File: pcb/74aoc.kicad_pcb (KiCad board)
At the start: 2 copper layers, 72 parts, among them J1 Conn_01x02_Pin, J2 Conn_01x06_Pin, U1 MC74HC151ADTR2G, U2 SN74LVC1G74, U3 AMS1117-3.3, U5 SN74HC595PWR, U6 SN74HC595PWR

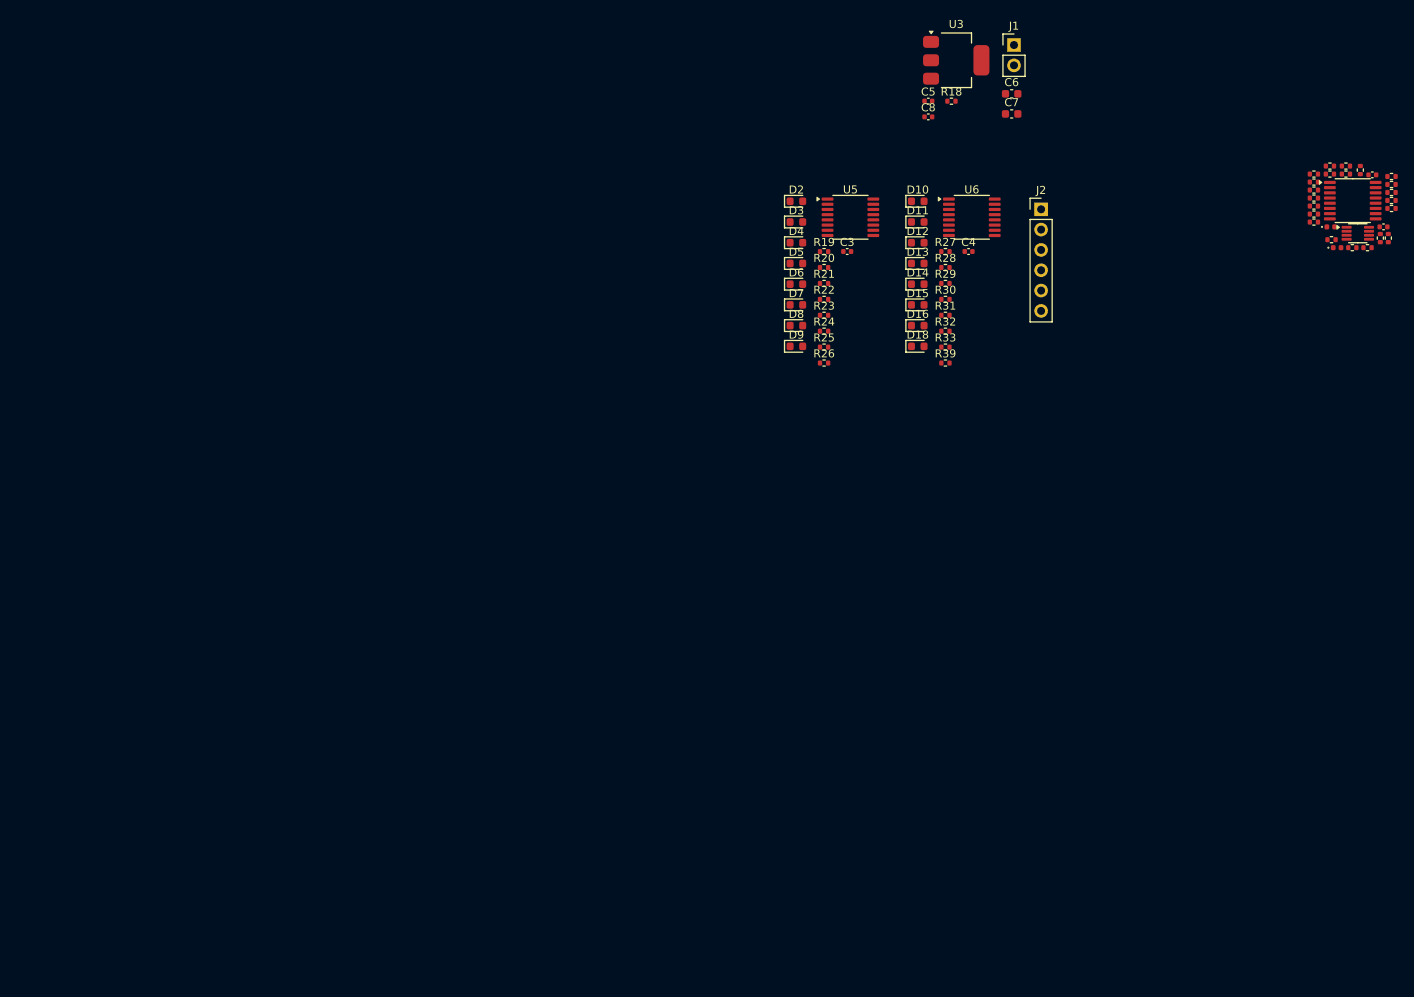
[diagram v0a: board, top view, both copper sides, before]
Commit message: Remove IO shift registers
Too complex
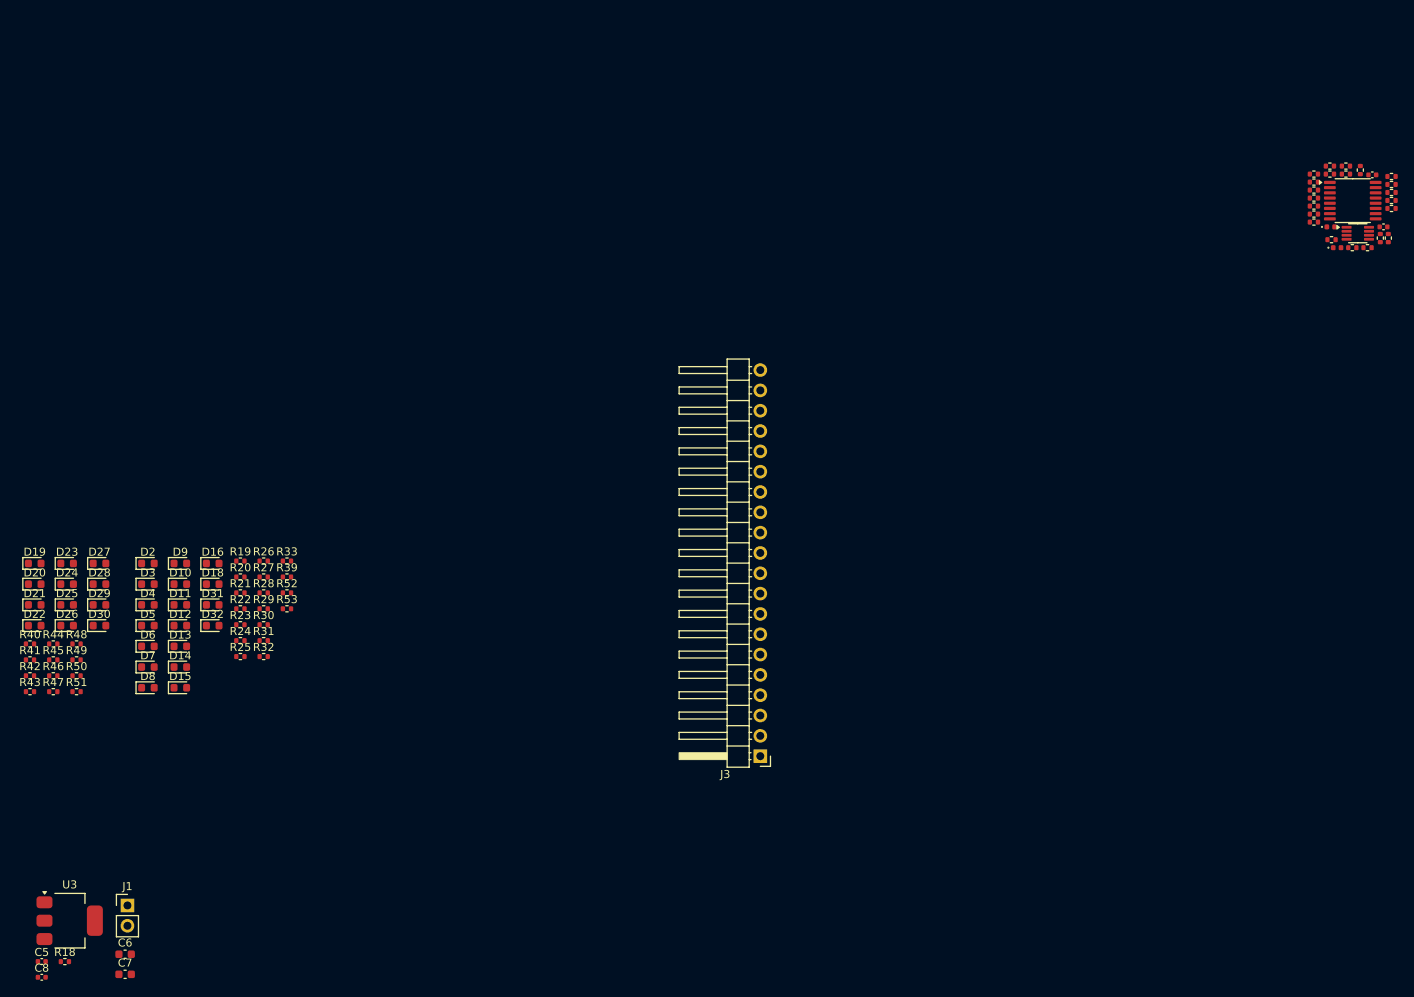
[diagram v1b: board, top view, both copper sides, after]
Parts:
- removed C3, C4: 100n, Capacitor_SMD:C_0402_1005Metric
- removed J2: Conn_01x06_Pin, Connector_PinHeader_2.54mm:PinHeader_1x06_P2.54mm_Vertical
- removed U5, U6: SN74HC595PWR, Package_SO:TSSOP-16_4.4x5mm_P0.65mm
- added D19: LED, LED_SMD:LED_0603_1608Metric, F.Cu at (-59.0, 143.4)
- added D20: LED, LED_SMD:LED_0603_1608Metric, F.Cu at (-59.0, 146.0)
- added D21: LED, LED_SMD:LED_0603_1608Metric, F.Cu at (-59.0, 148.6)
- added D22: LED, LED_SMD:LED_0603_1608Metric, F.Cu at (-59.0, 151.1)
- added D23: LED, LED_SMD:LED_0603_1608Metric, F.Cu at (-55.0, 143.4)
- added D24: LED, LED_SMD:LED_0603_1608Metric, F.Cu at (-55.0, 146.0)
- added D25: LED, LED_SMD:LED_0603_1608Metric, F.Cu at (-55.0, 148.6)
- added D26: LED, LED_SMD:LED_0603_1608Metric, F.Cu at (-55.0, 151.1)
- added D27: LED, LED_SMD:LED_0603_1608Metric, F.Cu at (-50.9, 143.4)
- added D28: LED, LED_SMD:LED_0603_1608Metric, F.Cu at (-50.9, 146.0)
- added D29: LED, LED_SMD:LED_0603_1608Metric, F.Cu at (-50.9, 148.6)
- added D30: LED, LED_SMD:LED_0603_1608Metric, F.Cu at (-50.9, 151.1)
- added D31: LED, LED_SMD:LED_0603_1608Metric, F.Cu at (-36.8, 148.6)
- added D32: LED, LED_SMD:LED_0603_1608Metric, F.Cu at (-36.8, 151.1)
- added J3: Conn_01x20_Pin, Connector_PinHeader_2.54mm:PinHeader_1x20_P2.54mm_Horizontal, F.Cu at (31.7, 167.5)
- added R40: 10k, Resistor_SMD:R_0402_1005Metric, F.Cu at (-59.6, 153.4)
- added R41: 10k, Resistor_SMD:R_0402_1005Metric, F.Cu at (-59.6, 155.4)
- added R42: 10k, Resistor_SMD:R_0402_1005Metric, F.Cu at (-59.6, 157.4)
- added R43: 10k, Resistor_SMD:R_0402_1005Metric, F.Cu at (-59.6, 159.4)
- added R44: 10k, Resistor_SMD:R_0402_1005Metric, F.Cu at (-56.7, 153.4)
- added R45: 10k, Resistor_SMD:R_0402_1005Metric, F.Cu at (-56.7, 155.4)
- added R46: 10k, Resistor_SMD:R_0402_1005Metric, F.Cu at (-56.7, 157.4)
- added R47: 10k, Resistor_SMD:R_0402_1005Metric, F.Cu at (-56.7, 159.4)
- added R48: 10k, Resistor_SMD:R_0402_1005Metric, F.Cu at (-53.8, 153.4)
- added R49: 10k, Resistor_SMD:R_0402_1005Metric, F.Cu at (-53.8, 155.4)
- added R50: 10k, Resistor_SMD:R_0402_1005Metric, F.Cu at (-53.8, 157.4)
- added R51: 10k, Resistor_SMD:R_0402_1005Metric, F.Cu at (-53.8, 159.4)
- added R52: 10k, Resistor_SMD:R_0402_1005Metric, F.Cu at (-27.5, 147.1)
- added R53: 10k, Resistor_SMD:R_0402_1005Metric, F.Cu at (-27.5, 149.0)
- moved C5 154.4 mm to (-58.1, 193.1)
- moved C6 154.4 mm to (-47.7, 192.2)
- moved C7 154.4 mm to (-47.7, 194.7)
- moved C8 154.4 mm to (-58.1, 195.1)
- moved J1 154.4 mm to (-47.4, 186.1)
- moved R18 154.4 mm to (-55.2, 193.1)
- moved U3 154.4 mm to (-54.6, 188.0)
- moved D10 103.9 mm to (-40.8, 146.0)
- moved D11 103.9 mm to (-40.8, 148.6)
- moved D14 103.9 mm to (-40.8, 156.3)
- moved D15 103.9 mm to (-40.8, 158.9)
- moved D12 103.9 mm to (-40.8, 151.1)
- moved D13 103.9 mm to (-40.8, 153.7)
- moved R28 94.4 mm to (-30.4, 147.1)
- moved R31 94.4 mm to (-30.4, 153.0)
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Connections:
- R19 pad 1: W_IO_O1 -> W_IO_I0
- R20 pad 1: W_IO_O2 -> W_IO_I1
- R21 pad 1: W_IO_O3 -> W_IO_I2
- R22 pad 1: W_IO_O4 -> W_IO_I3
- R23 pad 1: W_IO_O5 -> W_IO_I4
- R24 pad 1: W_IO_O6 -> W_IO_I5
- R25 pad 1: W_IO_O7 -> W_IO_I6
- R26 pad 1: W_IO_O0 -> W_IO_I7
- R27 pad 1: W_IO_O9 -> W_IO_I8
- R28 pad 1: W_IO_O10 -> W_IO_I9
- R29 pad 1: W_IO_O11 -> W_IO_I10
- R30 pad 1: W_IO_O12 -> W_IO_I11
- R31 pad 1: W_IO_O13 -> W_IO_I12
- R32 pad 1: W_IO_O14 -> W_IO_I13
- R33 pad 1: W_IO_O15 -> W_IO_I14
- R39 pad 1: W_IO_O8 -> W_IO_I15
